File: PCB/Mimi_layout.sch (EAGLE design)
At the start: 13 parts

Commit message: Layout V2
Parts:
- added C1: 10uF, SparkFun:CAP_POL1206
- added C2: 68uF, SparkFun:CAP_POL3528
- added D1: MBRA140, SparkFun:DIODESMA
- added L1: 47uH, SparkFun:INDUCTORCR54
- added R1: 1K, resistor:R-US_R0805
- added R2: 1.56k, resistor:R-US_R0805
- added U1: NCP1402, SparkFun:V_REG_NCP1400SOT23-5
- added U2: V_REG_317SMD, SparkFun-PowerIC:V_REG_317SMD
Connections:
- removed net MKR_GND: MKR1000_LEFT.4
- new net N$2: R1.1, R2.2, U2.ADJ
- new net N$3: D1.A, L1.2, U1.LX
- new net PM_OUT: SHINYEI.1, U2.IN
- new net V_5: C2.+, D1.C, EC4-500.1, FAN.1, SHINYEI.2, U1.EN, U1.OUT
- net GND: now also C1.-, C2.-, FAN.2, MKR1000_LEFT.4, R2.1, U1.GND
- net MKR_0: now also R1.2, U2.OUT; no longer SHINYEI.1
- net MKR_5V: no longer EC4-500.1, FAN.1, SHINYEI.2
- net MKR_VCC: now also C1.+, L1.1
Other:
- note added: "5v Supply"
- moved on the sheet: FAN

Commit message: Board V3
Version 3 of the schematic and board. might be able to shrink a little more but everything is pretty tight as is.
Also added EPL LPKF CAM/DRU files for making GBRs for manufacturing and ensuring the layout does not violate machine tolerances
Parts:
- added C3, C4: 100nf, SparkFun:CAP_POL1206
- added IC1, IC2, IC3: AD820N, analog-devices:AD820N
- added R14, R15, R18, R6, R7: 10k, resistor:R-US_R0805
- added R16, R17: 10, resistor:R-US_R0805
- added R19, R3, R4, R5: 330, resistor:R-US_R0805
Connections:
- new net CO_C: C4.-, EC4-500.2, IC1.OUT
- new net CO_R: EC4-500.3, R6.1
- new net CO_S: EC4-500.1, R16.2
- new net N$10: IC3.IN+, R3.2, R5.2
- new net N$11: IC3.IN-, R19.1, R4.2
- new net N$4: C4.+, R6.2, R7.1
- new net N$5: IC1.IN+, R14.2, R17.1, R4.1
- new net N$6: IC1.IN-, R7.2
- new net N$7: IC2.IN+, R17.2
- new net N$8: C3.-, IC2.IN-, R16.1, R18.1
- new net N$9: C3.+, IC2.OUT, R18.2, R3.1
- net GND: now also IC1.-VS, IC2.-VS, IC3.-VS, R15.1, R5.1; no longer EC4-500.3
- net MKR_A3: now also IC3.OUT, R19.2; no longer EC4-500.2
- net V_5: now also IC1.+VS, IC2.+VS, IC3.+VS, R14.1, R15.2; no longer EC4-500.1

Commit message: compression & schematic fixes
board dimensions shrunk to 2.18 * 1.62. will try to compress further but from this point on there will be diminishing returns on time spent vs   resulting compression.

also fixed a few warnings in schematic capture mode. there are still some but none are serious problems.
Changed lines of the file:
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@@
 <wire x1="167.64" y1="88.9" x2="170.18" y2="91.44" width="0.1524" layer="91"/>
 <label x="170.18" y="91.44" size="1.778" layer="95"/>
+<junction x="167.64" y="81.28"/>
 </segment>
 </net>
@@
 <wire x1="38.1" y1="-48.26" x2="38.1" y2="-66.04" width="0.1524" layer="91"/>
 <label x="60.96" y="-66.04" size="1.778" layer="95"/>
+<junction x="38.1" y="-66.04"/>
 </segment>
 </net>
@@
 <wire x1="142.24" y1="106.68" x2="142.24" y2="111.76" width="0.1524" layer="91"/>
 <label x="142.24" y="111.76" size="1.778" layer="95"/>
+<junction x="142.24" y="106.68"/>
 </segment>
 <segment>
@@
 <wire x1="93.98" y1="-2.54" x2="93.98" y2="0" width="0.1524" layer="91"/>
 <label x="93.98" y="0" size="1.778" layer="95"/>
+<junction x="93.98" y="-2.54"/>
 </segment>
 <segment>
@@
 <pinref part="R2" gate="G$1" pin="2"/>
 <wire x1="111.76" y1="76.2" x2="111.76" y2="73.66" width="0.1524" layer="91"/>
+<junction x="111.76" y="76.2"/>
 </segment>
 </net>
@@
 <pinref part="EC4-500" gate="A" pin="2"/>
 <wire x1="30.48" y1="0" x2="-12.7" y2="0" width="0.1524" layer="91"/>
+<junction x="30.48" y="0"/>
 </segment>
 </net>
@@
 <wire x1="30.48" y1="10.16" x2="50.8" y2="10.16" width="0.1524" layer="91"/>
 <pinref part="R7" gate="G$1" pin="1"/>
+<junction x="30.48" y="10.16"/>
 </segment>
 </net>
@@
 <wire x1="-5.08" y1="-43.18" x2="78.74" y2="-43.18" width="0.1524" layer="91"/>
 <wire x1="78.74" y1="-43.18" x2="78.74" y2="-30.48" width="0.1524" layer="91"/>
+<junction x="78.74" y="-30.48"/>
+<junction x="78.74" y="-2.54"/>
 </segment>
 </net>
@@
 <wire x1="5.08" y1="-17.78" x2="5.08" y2="-25.4" width="0.1524" layer="91"/>
 <wire x1="5.08" y1="-17.78" x2="2.54" y2="-17.78" width="0.1524" layer="91"/>
+<junction x="5.08" y="-17.78"/>
+<junction x="35.56" y="-25.4"/>
 </segment>
 </net>
@@
 <wire x1="-12.7" y1="-30.48" x2="-12.7" y2="-68.58" width="0.1524" layer="91"/>
 <pinref part="R3" gate="G$1" pin="1"/>
+<junction x="-12.7" y="-25.4"/>
+<junction x="-12.7" y="-30.48"/>
 </segment>
 </net>
@@
 <pinref part="IC3" gate="G$1" pin="IN+"/>
 <wire x1="0" y1="-68.58" x2="7.62" y2="-68.58" width="0.1524" layer="91"/>
+<junction x="0" y="-68.58"/>
 </segment>
 </net>
@@
 <pinref part="R19" gate="G$1" pin="1"/>
 <wire x1="5.08" y1="-48.26" x2="27.94" y2="-48.26" width="0.1524" layer="91"/>
-</segment>
-</net>
+<junction x="5.08" y="-63.5"/>
+</segment>
+</net>

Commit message: capacitor fix
removed oversize capacitors (1206) and replaced with 0805s
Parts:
- removed C1: 10uF, SparkFun:CAP_POL1206
- removed C2: 68uF, SparkFun:CAP_POL3528
- removed C3, C4: 100nf, SparkFun:CAP_POL1206
- added C5, C8: 100nf, resistor:C-USC0805
- added C6: 68uf, resistor:C-USC0805
- added C9: 10uf, resistor:C-USC0805
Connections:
- net CO_C: now also C5.2; no longer C4.-
- net GND: now also C6.2, C9.2; no longer C1.-, C2.-
- net MKR_VCC: now also C9.1; no longer C1.+
- net N$4: now also C5.1; no longer C4.+
- net N$8: now also C8.2; no longer C3.-
- net N$9: now also C8.1; no longer C3.+
- net V_3.3: no longer R10.1, R9.1
- net V_5: now also C6.1, R10.1, R9.1; no longer C2.+
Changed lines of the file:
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@@
 <part name="U1" library="SparkFun" deviceset="V_REG_NCP1400" device="SOT23-5" value="NCP1402"/>
 <part name="D1" library="SparkFun" deviceset="DIODE" device="SMA" value="MBRA140"/>
-<part name="C1" library="SparkFun" deviceset="CAP_POL" device="1206" value="10uF"/>
-<part name="C2" library="SparkFun" deviceset="CAP_POL" device="3528" value="68uF"/>
 <part name="L1" library="SparkFun" deviceset="INDUCTOR" device="CR54" value="47uH"/>
 <part name="GND8" library="SparkFun" deviceset="GND" device=""/>
@@
 <part name="IC3" library="analog-devices" deviceset="AD820N" device=""/>
 <part name="R3" library="resistor" deviceset="R-US_" device="R0805" value="330"/>
-<part name="C3" library="SparkFun" deviceset="CAP_POL" device="1206" value="100nf"/>
 <part name="R5" library="resistor" deviceset="R-US_" device="R0805" value="330"/>
-<part name="C4" library="SparkFun" deviceset="CAP_POL" device="1206" value="100nf"/>
 <part name="R6" library="resistor" deviceset="R-US_" device="R0805" value="10k"/>
 <part name="R7" library="resistor" deviceset="R-US_" device="R0805" value="10k"/>
@@
 <part name="GND14" library="SparkFun-Aesthetics" deviceset="GND" device=""/>
 <part name="GND15" library="SparkFun-Aesthetics" deviceset="GND" device=""/>
+<part name="C5" library="resistor" deviceset="C-US" device="C0805" value="100nf"/>
+<part name="C6" library="resistor" deviceset="C-US" device="C0805" value="68uf"/>
+<part name="C8" library="resistor" deviceset="C-US" device="C0805" value="100nf"/>
+<part name="C9" library="resistor" deviceset="C-US" device="C0805" value="10uf"/>
 </parts>
 <sheets>
@@
 <attribute name="VALUE" x="246.38" y="111.9886" size="1.778" layer="96"/>
 </instance>
-<instance part="C1" gate="G$1" x="208.28" y="96.52"/>
-<instance part="C2" gate="G$1" x="266.7" y="96.52"/>
 <instance part="L1" gate="G$1" x="220.98" y="101.6" smashed="yes" rot="R90">
 <attribute name="NAME" x="218.44" y="104.14" size="1.778" layer="95"/>
@@
 <instance part="IC3" gate="G$1" x="12.7" y="-66.04" rot="MR180"/>
 <instance part="R3" gate="G$1" x="-7.62" y="-68.58"/>
-<instance part="C3" gate="G$1" x="-2.54" y="-17.78" rot="R90"/>
 <instance part="R5" gate="G$1" x="0" y="-76.2" rot="R90"/>
-<instance part="C4" gate="G$1" x="30.48" y="7.62"/>
 <instance part="R6" gate="G$1" x="15.24" y="10.16"/>
 <instance part="R7" gate="G$1" x="55.88" y="10.16"/>
@@
 <instance part="GND14" gate="1" x="76.2" y="10.16"/>
 <instance part="GND15" gate="1" x="22.86" y="-58.42"/>
+<instance part="C5" gate="G$1" x="30.48" y="7.62"/>
+<instance part="C6" gate="G$1" x="266.7" y="96.52"/>
+<instance part="C8" gate="G$1" x="-2.54" y="-17.78" rot="R90"/>
+<instance part="C9" gate="G$1" x="208.28" y="96.52"/>
 </instances>
 <busses>
@@
 <label x="198.12" y="101.6" size="1.778" layer="95"/>
 <pinref part="L1" gate="G$1" pin="1"/>
-<pinref part="C1" gate="G$1" pin="+"/>
+<pinref part="C9" gate="G$1" pin="1"/>
 </segment>
 </net>
@@
 <net name="V_3.3" class="0">
 <segment>
-<pinref part="R9" gate="G$1" pin="1"/>
-<wire x1="137.16" y1="104.14" x2="137.16" y2="106.68" width="0.1524" layer="91"/>
-<wire x1="137.16" y1="106.68" x2="142.24" y2="106.68" width="0.1524" layer="91"/>
-<pinref part="R10" gate="G$1" pin="1"/>
-<wire x1="142.24" y1="106.68" x2="147.32" y2="106.68" width="0.1524" layer="91"/>
-<wire x1="147.32" y1="106.68" x2="147.32" y2="104.14" width="0.1524" layer="91"/>
-<wire x1="142.24" y1="106.68" x2="142.24" y2="111.76" width="0.1524" layer="91"/>
-<label x="142.24" y="111.76" size="1.778" layer="95"/>
-<junction x="142.24" y="106.68"/>
-</segment>
-<segment>
 <wire x1="25.4" y1="66.04" x2="33.02" y2="66.04" width="0.1524" layer="91"/>
 <label x="33.02" y="66.04" size="1.778" layer="95"/>
@@
 <segment>
 <wire x1="266.7" y1="91.44" x2="266.7" y2="88.9" width="0.1524" layer="91"/>
-<pinref part="C2" gate="G$1" pin="-"/>
 <pinref part="GND10" gate="1" pin="GND"/>
+<pinref part="C6" gate="G$1" pin="2"/>
 </segment>
 <segment>
@@
 <segment>
 <wire x1="208.28" y1="91.44" x2="208.28" y2="88.9" width="0.1524" layer="91"/>
-<pinref part="C1" gate="G$1" pin="-"/>
 <pinref part="GND8" gate="1" pin="GND"/>
+<pinref part="C9" gate="G$1" pin="2"/>
 </segment>
 <segment>
@@
 <pinref part="U1" gate="G$1" pin="OUT"/>
 <pinref part="D1" gate="G$1" pin="C"/>
-<pinref part="C2" gate="G$1" pin="+"/>
+<pinref part="C6" gate="G$1" pin="1"/>
 </segment>
 <segment>
@@
 <wire x1="12.7" y1="-76.2" x2="12.7" y2="-78.74" width="0.1524" layer="91"/>
 <label x="12.7" y="-78.74" size="1.778" layer="95"/>
+</segment>
+<segment>
+<pinref part="R9" gate="G$1" pin="1"/>
+<wire x1="137.16" y1="104.14" x2="137.16" y2="106.68" width="0.1524" layer="91"/>
+<wire x1="137.16" y1="106.68" x2="142.24" y2="106.68" width="0.1524" layer="91"/>
+<pinref part="R10" gate="G$1" pin="1"/>
+<wire x1="142.24" y1="106.68" x2="147.32" y2="106.68" width="0.1524" layer="91"/>
+<wire x1="147.32" y1="106.68" x2="147.32" y2="104.14" width="0.1524" layer="91"/>
+<wire x1="142.24" y1="106.68" x2="142.24" y2="111.76" width="0.1524" layer="91"/>
+<junction x="142.24" y="106.68"/>
 </segment>
 </net>
@@
 <label x="0" y="0" size="1.778" layer="95"/>
 <wire x1="30.48" y1="2.54" x2="30.48" y2="0" width="0.1524" layer="91"/>
-<pinref part="C4" gate="G$1" pin="-"/>
 <pinref part="IC1" gate="G$1" pin="OUT"/>
 <wire x1="60.96" y1="0" x2="30.48" y2="0" width="0.1524" layer="91"/>
@@
 <wire x1="30.48" y1="0" x2="-12.7" y2="0" width="0.1524" layer="91"/>
 <junction x="30.48" y="0"/>
+<pinref part="C5" gate="G$1" pin="2"/>
 </segment>
 </net>
@@
 <net name="N$4" class="0">
 <segment>
-<pinref part="C4" gate="G$1" pin="+"/>
 <pinref part="R6" gate="G$1" pin="2"/>
-<wire x1="30.48" y1="10.16" x2="20.32" y2="10.16" width="0.1524" layer="91"/>
+<wire x1="20.32" y1="10.16" x2="30.48" y2="10.16" width="0.1524" layer="91"/>
+<pinref part="R7" gate="G$1" pin="1"/>
+<pinref part="C5" gate="G$1" pin="1"/>
 <wire x1="30.48" y1="10.16" x2="50.8" y2="10.16" width="0.1524" layer="91"/>
-<pinref part="R7" gate="G$1" pin="1"/>
 <junction x="30.48" y="10.16"/>
 </segment>
@@
 <wire x1="2.54" y1="-25.4" x2="5.08" y2="-25.4" width="0.1524" layer="91"/>
 <wire x1="5.08" y1="-10.16" x2="5.08" y2="-17.78" width="0.1524" layer="91"/>
-<pinref part="C3" gate="G$1" pin="-"/>
 <wire x1="5.08" y1="-17.78" x2="5.08" y2="-25.4" width="0.1524" layer="91"/>
 <wire x1="5.08" y1="-17.78" x2="2.54" y2="-17.78" width="0.1524" layer="91"/>
 <junction x="5.08" y="-17.78"/>
 <junction x="35.56" y="-25.4"/>
+<pinref part="C8" gate="G$1" pin="2"/>
 </segment>
 </net>
 <net name="N$9" class="0">
 <segment>
-<pinref part="C3" gate="G$1" pin="+"/>
 <wire x1="-5.08" y1="-17.78" x2="-12.7" y2="-17.78" width="0.1524" layer="91"/>
 <wire x1="-12.7" y1="-17.78" x2="-12.7" y2="-25.4" width="0.1524" layer="91"/>
@@
 <junction x="-12.7" y="-25.4"/>
 <junction x="-12.7" y="-30.48"/>
-</segment>
-</net>
+<pinref part="C8" gate="G$1" pin="1"/>
+</segment>
+</net>

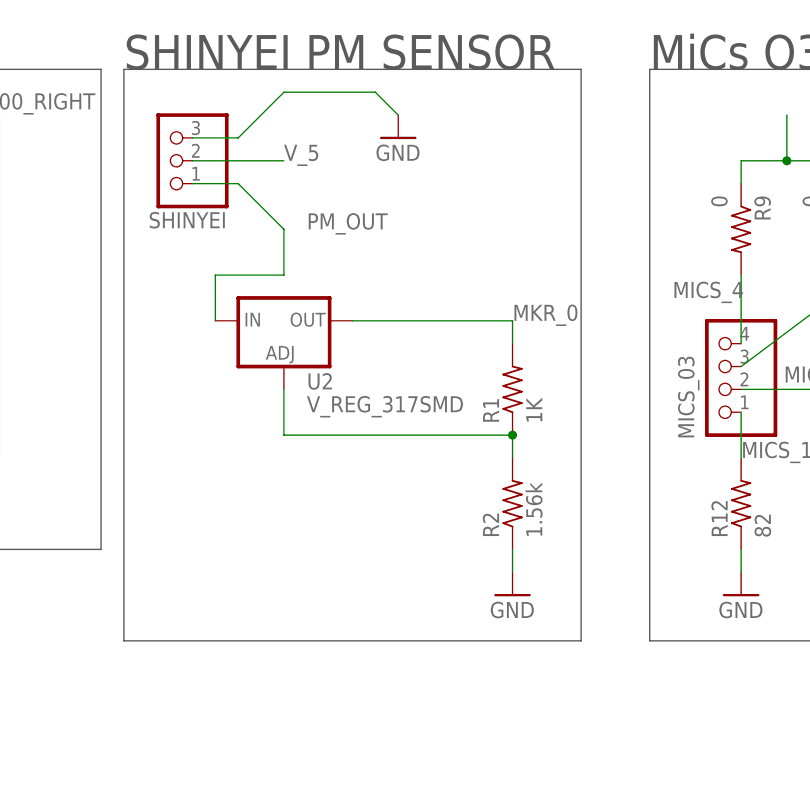
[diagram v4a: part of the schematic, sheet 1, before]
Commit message: replaced components, rerouted
a few components were removed and resistances changed in accordance with observed device behavior
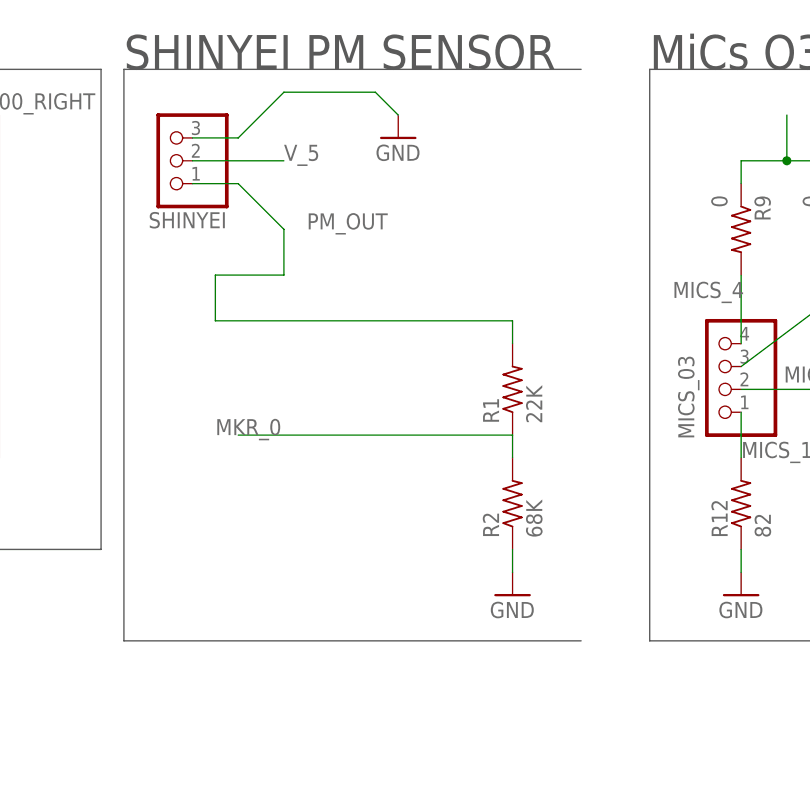
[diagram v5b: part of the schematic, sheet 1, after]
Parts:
- removed U2: V_REG_317SMD, SparkFun-PowerIC:V_REG_317SMD
- R1: value 1K -> 22K
- R2: value 1.56k -> 68K
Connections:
- removed net N$2: R1.1, R2.2, U2.ADJ
- net MKR_0: now also R1.1, R2.2; no longer R1.2, U2.OUT
- net PM_OUT: now also R1.2; no longer U2.IN
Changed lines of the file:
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@@
 <part name="GND10" library="SparkFun" deviceset="GND" device=""/>
 <part name="GND7" library="SparkFun-Aesthetics" deviceset="GND" device=""/>
-<part name="U2" library="SparkFun-PowerIC" deviceset="V_REG_317" device="SMD"/>
-<part name="R1" library="resistor" deviceset="R-US_" device="R0805" value="1K"/>
-<part name="R2" library="resistor" deviceset="R-US_" device="R0805" value="1.56k"/>
+<part name="R1" library="resistor" deviceset="R-US_" device="R0805" value="22K"/>
+<part name="R2" library="resistor" deviceset="R-US_" device="R0805" value="68K"/>
 <part name="GND11" library="SparkFun-Aesthetics" deviceset="GND" device=""/>
 <part name="IC1" library="analog-devices" deviceset="AD820N" device=""/>
@@
 <wire x1="279.4" y1="116.84" x2="195.58" y2="116.84" width="0.1524" layer="97"/>
 <text x="195.58" y="116.84" size="3.81" layer="97">5v Supply</text>
-<wire x1="119.38" y1="116.84" x2="119.38" y2="53.34" width="0.1524" layer="97"/>
 <wire x1="119.38" y1="53.34" x2="68.58" y2="53.34" width="0.1524" layer="97"/>
 <wire x1="68.58" y1="53.34" x2="68.58" y2="116.84" width="0.1524" layer="97"/>
@@
 <instance part="GND10" gate="1" x="266.7" y="86.36"/>
 <instance part="GND7" gate="1" x="20.32" y="81.28"/>
-<instance part="U2" gate="G$1" x="86.36" y="88.9"/>
 <instance part="R1" gate="G$1" x="111.76" y="81.28" rot="R90"/>
 <instance part="R2" gate="G$1" x="111.76" y="68.58" rot="R90"/>
@@
 </segment>
 <segment>
-<pinref part="U2" gate="G$1" pin="OUT"/>
-<wire x1="93.98" y1="88.9" x2="111.76" y2="88.9" width="0.1524" layer="91"/>
-<pinref part="R1" gate="G$1" pin="2"/>
-<wire x1="111.76" y1="88.9" x2="111.76" y2="86.36" width="0.1524" layer="91"/>
-<label x="111.76" y="88.9" size="1.778" layer="95"/>
+<pinref part="R1" gate="G$1" pin="1"/>
+<pinref part="R2" gate="G$1" pin="2"/>
+<wire x1="111.76" y1="76.2" x2="111.76" y2="73.66" width="0.1524" layer="91"/>
+<wire x1="111.76" y1="76.2" x2="81.28" y2="76.2" width="0.1524" layer="91"/>
+<label x="78.74" y="76.2" size="1.778" layer="95"/>
 </segment>
 </net>
@@
 </segment>
 </net>
-<net name="N$2" class="0">
-<segment>
-<pinref part="R1" gate="G$1" pin="1"/>
-<wire x1="111.76" y1="76.2" x2="86.36" y2="76.2" width="0.1524" layer="91"/>
-<pinref part="U2" gate="G$1" pin="ADJ"/>
-<wire x1="86.36" y1="76.2" x2="86.36" y2="81.28" width="0.1524" layer="91"/>
-<pinref part="R2" gate="G$1" pin="2"/>
-<wire x1="111.76" y1="76.2" x2="111.76" y2="73.66" width="0.1524" layer="91"/>
-<junction x="111.76" y="76.2"/>
-</segment>
-</net>
 <net name="PM_OUT" class="0">
 <segment>
-<pinref part="U2" gate="G$1" pin="IN"/>
 <wire x1="78.74" y1="88.9" x2="78.74" y2="93.98" width="0.1524" layer="91"/>
 <pinref part="SHINYEI" gate="A" pin="1"/>
@@
 <wire x1="78.74" y1="93.98" x2="86.36" y2="93.98" width="0.1524" layer="91"/>
 <wire x1="86.36" y1="93.98" x2="86.36" y2="99.06" width="0.1524" layer="91"/>
-</segment>
-</net>
+<pinref part="R1" gate="G$1" pin="2"/>
+<wire x1="78.74" y1="88.9" x2="111.76" y2="88.9" width="0.1524" layer="91"/>
+<wire x1="111.76" y1="88.9" x2="111.76" y2="86.36" width="0.1524" layer="91"/>
+</segment>
+</net>
